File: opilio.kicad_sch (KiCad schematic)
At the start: 85 parts, among them J1 DB301V-5.0-2P, J2 USB_C_Receptacle_USB2.0, J6 Conn_01x06_Male, Q1 CJ3134KW, Q2 NCE30P30K, SW1 Reset, SW2 Boot, U1 EUP3458, U2 STM32F103C8T6, U3 USBLC6-2SC6, Y1 TAXM8M4RFDCET2T, Y2 YST310S 32.768KHz

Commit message: initial routing
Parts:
- removed J1: DB301V-5.0-2P, easyeda2kicad:CONN-TH_2P-P5.00_L7.6-W10.0, symbol easyeda:DB301V-5.0-2P
- added J1: SATA_Power_Connector, Custom:Sata_Power_Connector_SMD, symbol Custom:SATA_Power_Connector
- added J3: Conn_01x04_Male, Connector_PinHeader_2.54mm:PinHeader_1x04_P2.54mm_Vertical, symbol Connector:Conn_01x04_Male
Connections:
- net +12V: now also J1.13 (precharge_12V), J1.14 (12V), J1.15 (12V)
- net +3.3V: now also J3.1 (Pin_1)
- net GND: now also J1.10 (GND), J1.12 (GND), J1.4 (GND), J1.5 (GND), J1.6 (GND), J3.2 (Pin_2)
- net SWCLK: now also J3.3 (Pin_3)
- net SWIO: now also J3.4 (Pin_4)

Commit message: nearly ready
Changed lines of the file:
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@@
   (symbol (lib_id "Device:C_Small") (at 94.107 22.606 270) (unit 1)
     (in_bom yes) (on_board yes)
-    (property "Reference" "C5" (id 0) (at 94.996 17.907 0))
-    (property "Value" "10nF" (id 1) (at 92.964 18.161 0))
+    (property "Reference" "C5" (id 0) (at 93.726 17.145 90))
+    (property "Value" "10nF" (id 1) (at 93.98 19.177 90))
     (property "Footprint" "Capacitor_SMD:C_0402_1005Metric" (id 2) (at 94.107 22.606 0)
       (effects (font (size 1.27 1.27)) hide)

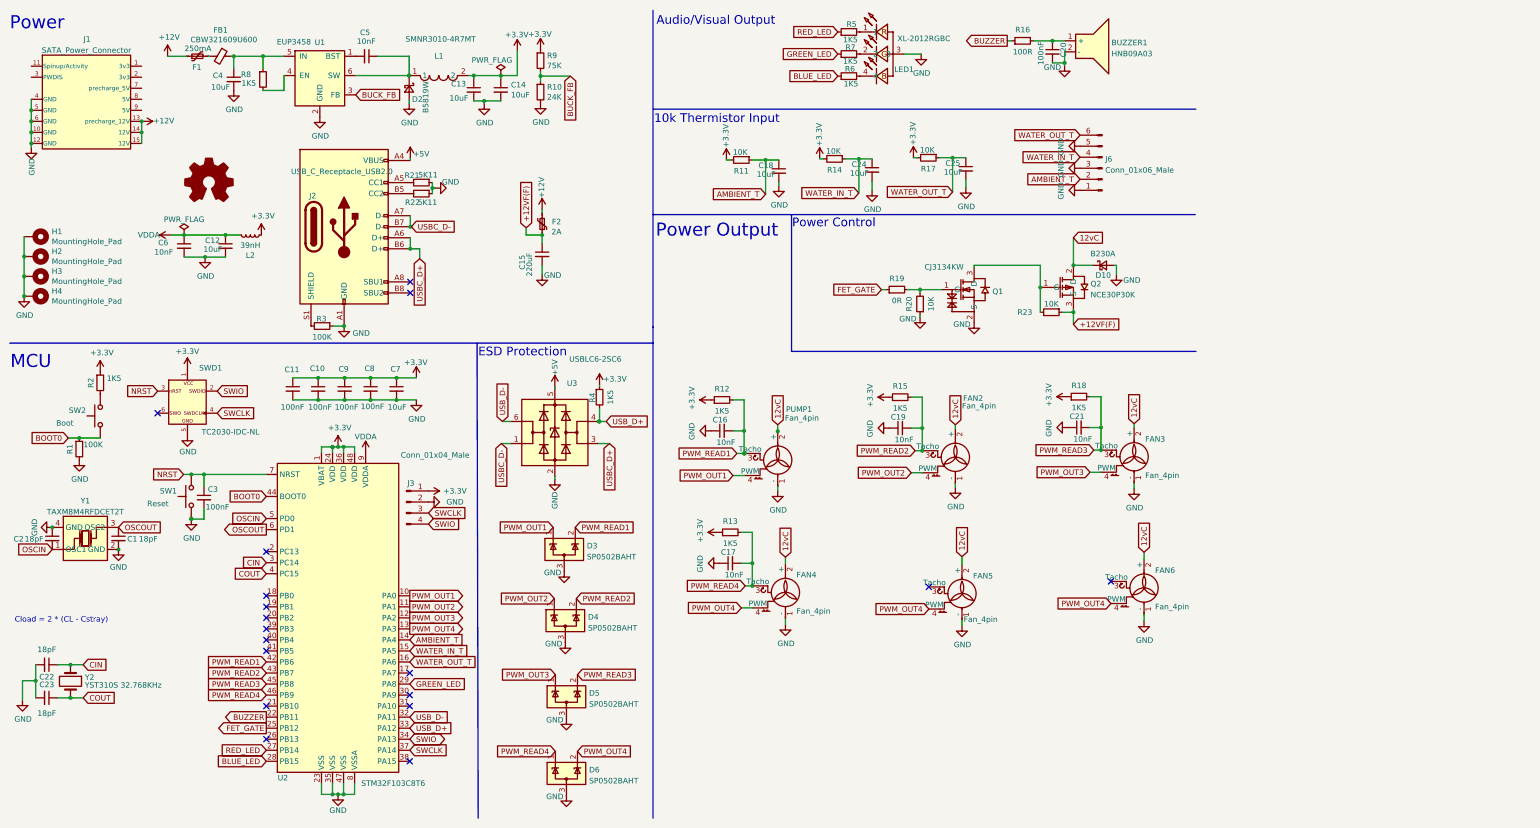
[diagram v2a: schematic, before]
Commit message: double mosfets
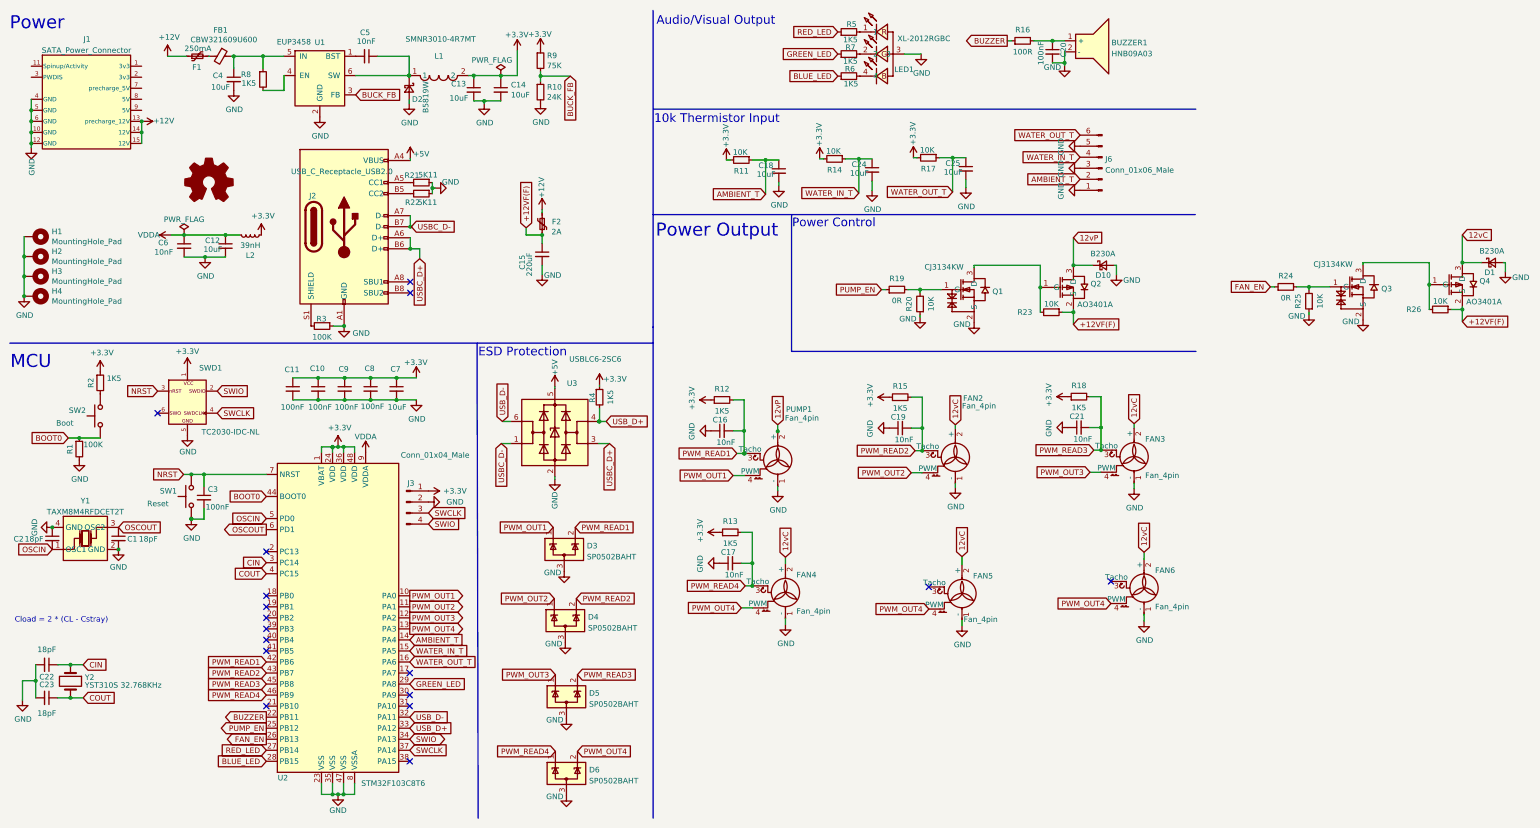
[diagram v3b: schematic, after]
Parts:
- removed Q2: NCE30P30K, easyeda2kicad:TO-252-2_L6.6-W6.1-P4.57-LS9.9-TL-CW, symbol easyeda:NCE30P30K
- added D1: B230A, Diode_SMD:D_SMA, symbol Device:D_Schottky_Small
- added Q2, Q4: AO3401A, easyeda2kicad:SOT-23_L2.9-W1.3-P1.90-LS2.4-BR, symbol easyeda:AO3401A
- added Q3: CJ3134KW, easyeda2kicad:SC-70-3_L2.1-W1.3-P1.30-LS2.1-BR, symbol easyeda:CJ3134KW
- added R24: 0R, Resistor_SMD:R_0402_1005Metric, symbol Device:R_Small
- added R25, R26: 10K, Resistor_SMD:R_0402_1005Metric, symbol Device:R_Small
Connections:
- net +12VF(F): now also Q2.2 (S), Q4.2 (S), R26.1
- net 12vC: now also D1.1 (K), Q4.3 (D); no longer D10.1 (K), PUMP1.2 (+)
- net GND: now also D1.2 (A), Q3.2 (S), R25.1
- net at Q1.3 (D), R23.2: now also Q2.1 (G)
- net FAN_EN: now reaches U2.26 (PB13)
- net FAN_EN: now also R24.1
- net FET_GATE renamed PUMP_EN
- new net: Q3.1 (G), R24.2, R25.2
- new net: Q3.3 (D), Q4.1 (G), R26.2
- new net 12vP: D10.1 (K), PUMP1.2 (+), Q2.3 (D)
- no-connect marks 18 -> 17

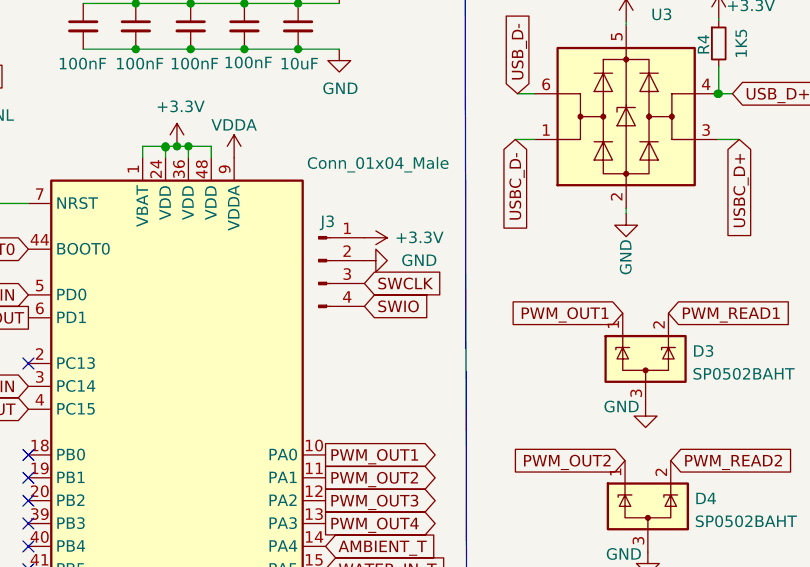
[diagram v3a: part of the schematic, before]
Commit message: match swd wires with bluepill
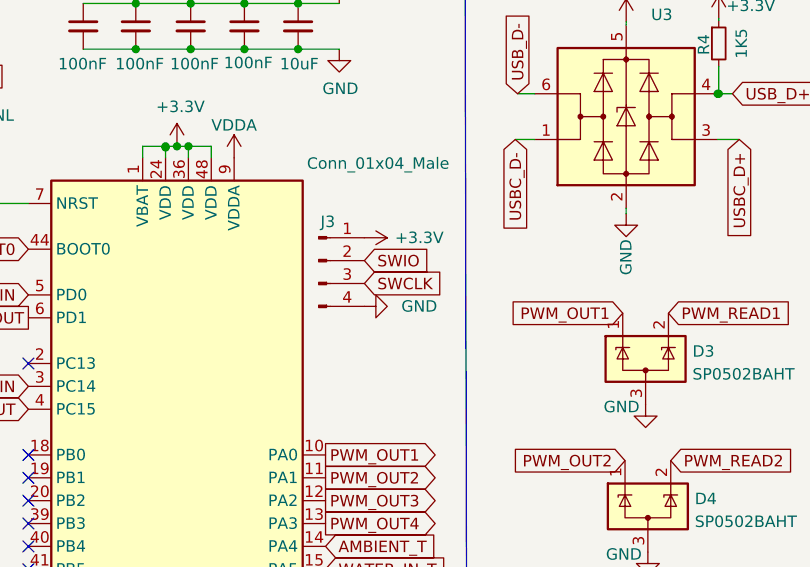
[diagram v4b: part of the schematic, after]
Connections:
- net GND: now also J3.4 (Pin_4); no longer J3.2 (Pin_2)
- net SWIO: now also J3.2 (Pin_2); no longer J3.4 (Pin_4)
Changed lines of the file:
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@@
     )
   )
-  (global_label "SWIO" (shape input) (at 108.331 130.302 0) (fields_autoplaced)
+  (global_label "SWIO" (shape input) (at 108.331 125.222 0) (fields_autoplaced)
     (effects (font (size 1.27 1.27)) (justify left))
-    (property "Intersheet References" "${INTERSHEET_REFS}" (id 0) (at 258.445 -146.812 0)
+    (property "Intersheet References" "${INTERSHEET_REFS}" (id 0) (at 258.445 -151.892 0)
       (effects (font (size 1.27 1.27)) hide)
     )
@@
     (pin "3")
   )
-  (symbol (lib_id "power:GND") (at 108.331 125.222 90) (unit 1)
+  (symbol (lib_id "power:GND") (at 108.331 130.302 90) (unit 1)
     (in_bom yes) (on_board yes)
-    (property "Reference" "#PWR06" (id 0) (at 114.681 125.222 0)
+    (property "Reference" "#PWR06" (id 0) (at 114.681 130.302 0)
       (effects (font (size 1.27 1.27)) hide)
     )
-    (property "Value" "GND" (id 1) (at 114.427 125.222 90))
-    (property "Footprint" "" (id 2) (at 108.331 125.222 0)
+    (property "Value" "GND" (id 1) (at 114.427 130.302 90))
+    (property "Footprint" "" (id 2) (at 108.331 130.302 0)
       (effects (font (size 1.27 1.27)) hide)
     )
-    (property "Datasheet" "" (id 3) (at 108.331 125.222 0)
+    (property "Datasheet" "" (id 3) (at 108.331 130.302 0)
       (effects (font (size 1.27 1.27)) hide)
     )

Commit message: before split schema
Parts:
- removed R2: 1K5, Resistor_SMD:R_0402_1005Metric, symbol Device:R_Small
- added C26: 100nF, Capacitor_SMD:C_0402_1005Metric, symbol Device:C_Small
- R1: value 100K -> 10K; LCSC Part C144792 -> C191123
- R3: value 100K -> 75K; LCSC Part C144792 -> C2689478
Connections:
- net +3.3V: now also SW2.2
- net BOOT0: now also C26.1
- net GND: now also C26.2
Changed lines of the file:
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@@
   (title_block
     (title "Opilio")
-    (date "2022-10-02")
-    (rev "6")
+    (date "2022-11-07")
+    (rev "7")
   )
   (junction (at 42.291 40.132) (diameter 0) (color 0 0 0 0)
@@
   (junction (at 221.488 76.327) (diameter 0) (color 0 0 0 0)
   )
+  (junction (at 32.766 110.49) (diameter 0) (color 0 0 0 0)
+  )
   (junction (at 104.14 66.929) (diameter 0) (color 0 0 0 0)
   )
@@
   (junction (at 180.975 108.839) (diameter 0) (color 0 0 0 0)
   )
+  (junction (at 30.226 115.57) (diameter 0) (color 0 0 0 0)
+  )
   (junction (at 16.891 42.672) (diameter 0) (color 0 0 0 0)
   )
@@
     (stroke (width 0) (type default) (color 0 0 0 0))
   )
+  (wire (pts (xy 30.226 115.57) (xy 27.94 115.57))
+    (stroke (width 0) (type default) (color 0 0 0 0))
+  )
   (wire (pts (xy 118.745 27.051) (xy 118.745 27.813))
     (stroke (width 0) (type default) (color 0 0 0 0))
@@
     (stroke (width 0) (type default) (color 0 0 0 0))
   )
+  (wire (pts (xy 30.226 115.57) (xy 32.766 115.57))
+    (stroke (width 0) (type default) (color 0 0 0 0))
+  )
   (wire (pts (xy 82.931 101.727) (xy 89.027 101.727))
     (stroke (width 0) (type default) (color 0 0 0 0))
@@
     (pin "1")
   )
-  (symbol (lib_id "power:GND") (at 27.94 115.57 0) (unit 1)
+  (symbol (lib_id "power:GND") (at 30.226 115.57 0) (unit 1)
     (in_bom yes) (on_board yes)
-    (property "Reference" "#PWR03" (id 0) (at 27.94 121.92 0)
+    (property "Reference" "#PWR03" (id 0) (at 30.226 121.92 0)
       (effects (font (size 1.27 1.27)) hide)
     )
-    (property "Value" "GND" (id 1) (at 28.067 119.9642 0))
-    (property "Footprint" "" (id 2) (at 27.94 115.57 0)
+    (property "Value" "GND" (id 1) (at 30.353 119.9642 0))
+    (property "Footprint" "" (id 2) (at 30.226 115.57 0)
       (effects (font (size 1.27 1.27)) hide)
     )
-    (property "Datasheet" "" (id 3) (at 27.94 115.57 0)
+    (property "Datasheet" "" (id 3) (at 30.226 115.57 0)
       (effects (font (size 1.27 1.27)) hide)
     )
@@
     (pin "1")
   )
-  (symbol (lib_id "power:+3.3V") (at 32.766 95.25 0) (unit 1)
+  (symbol (lib_id "power:+3.3V") (at 32.766 100.33 0) (unit 1)
     (in_bom yes) (on_board yes)
-    (property "Reference" "#PWR05" (id 0) (at 32.766 99.06 0)
+    (property "Reference" "#PWR05" (id 0) (at 32.766 104.14 0)
       (effects (font (size 1.27 1.27)) hide)
     )
-    (property "Value" "+3.3V" (id 1) (at 33.147 90.8558 0))
-    (property "Footprint" "" (id 2) (at 32.766 95.25 0)
+    (property "Value" "+3.3V" (id 1) (at 33.147 95.9358 0))
+    (property "Footprint" "" (id 2) (at 32.766 100.33 0)
       (effects (font (size 1.27 1.27)) hide)
     )
-    (property "Datasheet" "" (id 3) (at 32.766 95.25 0)
+    (property "Datasheet" "" (id 3) (at 32.766 100.33 0)
       (effects (font (size 1.27 1.27)) hide)
     )
@@
     (in_bom yes) (on_board yes)
     (property "Reference" "R3" (id 0) (at 83.693 83.058 90))
-    (property "Value" "100K" (id 1) (at 83.82 87.249 90))
+    (property "Value" "75K" (id 1) (at 83.82 87.249 90))
     (property "Footprint" "Resistor_SMD:R_0402_1005Metric" (id 2) (at 83.82 84.709 0)
       (effects (font (size 1.27 1.27)) hide)
@@
       (effects (font (size 1.27 1.27)) hide)
     )
-    (property "LCSC Part" "C144792" (id 4) (at 83.82 84.709 0)
+    (property "LCSC Part" "C2689478" (id 4) (at 83.82 84.709 0)
       (effects (font (size 1.27 1.27)) hide)
     )
@@
     (pin "2")
   )
+  (symbol (lib_id "Device:C_Small") (at 32.766 113.03 0) (unit 1)
+    (in_bom yes) (on_board yes)
+    (property "Reference" "C26" (id 0) (at 33.655 111.125 0)
+      (effects (font (size 1.27 1.27)) (justify left))
+    )
+    (property "Value" "100nF" (id 1) (at 33.147 115.189 0)
+      (effects (font (size 1.27 1.27)) (justify left))
+    )
+    (property "Footprint" "Capacitor_SMD:C_0402_1005Metric" (id 2) (at 32.766 113.03 0)
+      (effects (font (size 1.27 1.27)) hide)
+    )
+    (property "Datasheet" "~" (id 3) (at 32.766 113.03 0)
+      (effects (font (size 1.27 1.27)) hide)
+    )
+    (property "LCSC Part" "C100072" (id 4) (at 32.766 113.03 0)
+      (effects (font (size 1.27 1.27)) hide)
+    )
+    (pin "1")
+    (pin "2")
+  )
   (symbol (lib_id "Device:C_Small") (at 177.8 139.319 90) (unit 1)
     (in_bom yes) (on_board yes)
@@
     (in_bom yes) (on_board yes)
     (property "Reference" "R1" (id 0) (at 25.781 113.03 90))
-    (property "Value" "100K" (id 1) (at 31.115 112.014 0))
+    (property "Value" "10K" (id 1) (at 24.257 115.189 0))
     (property "Footprint" "Resistor_SMD:R_0402_1005Metric" (id 2) (at 27.94 113.03 0)
       (effects (font (size 1.27 1.27)) hide)
@@
       (effects (font (size 1.27 1.27)) hide)
     )
-    (property "LCSC Part" "C144792" (id 4) (at 27.94 113.03 0)
+    (property "LCSC Part" "C191123" (id 4) (at 27.94 113.03 0)
       (effects (font (size 1.27 1.27)) hide)
     )
@@
     (pin "2")
   )
-  (symbol (lib_id "Device:R_Small") (at 32.766 97.79 0) (unit 1)
-    (in_bom yes) (on_board yes)
-    (property "Reference" "R2" (id 0) (at 30.607 97.79 90))
-    (property "Value" "1K5" (id 1) (at 35.941 96.774 0))
-    (property "Footprint" "Resistor_SMD:R_0402_1005Metric" (id 2) (at 32.766 97.79 0)
-      (effects (font (size 1.27 1.27)) hide)
-    )
-    (property "Datasheet" "~" (id 3) (at 32.766 97.79 0)
-      (effects (font (size 1.27 1.27)) hide)
-    )
-    (property "LCSC Part" "C413084" (id 4) (at 32.766 97.79 0)
-      (effects (font (size 1.27 1.27)) hide)
-    )
-    (pin "1")
-    (pin "2")
-  )
   (symbol (lib_id "power:GND") (at 173.355 108.839 270) (unit 1)
     (in_bom yes) (on_board yes)
@@
       (reference "C25") (unit 1) (value "10uF") (footprint "Capacitor_SMD:C_0603_1608Metric")
     )
+    (path "/7a3f805d-442c-4192-9b77-8a7b61bfd9f5"
+      (reference "C26") (unit 1) (value "100nF") (footprint "Capacitor_SMD:C_0402_1005Metric")
+    )
     (path "/ff43c545-2e78-4ffc-ac31-897951bdbe96"
       (reference "D1") (unit 1) (value "B230A") (footprint "Diode_SMD:D_SMA")
@@
     )
     (path "/be987873-4856-4ad7-aaee-745ffdc5e733"
-      (reference "R1") (unit 1) (value "100K") (footprint "Resistor_SMD:R_0402_1005Metric")
-    )
-    (path "/c8fa8fa3-be95-4a0c-bb19-a1e338cef170"
-      (reference "R2") (unit 1) (value "1K5") (footprint "Resistor_SMD:R_0402_1005Metric")
+      (reference "R1") (unit 1) (value "10K") (footprint "Resistor_SMD:R_0402_1005Metric")
     )
     (path "/61dbdb34-0154-4f93-a2b2-aaae1dfa3913"
-      (reference "R3") (unit 1) (value "100K") (footprint "Resistor_SMD:R_0402_1005Metric")
+      (reference "R3") (unit 1) (value "75K") (footprint "Resistor_SMD:R_0402_1005Metric")
     )
     (path "/beb113ce-d7fe-47cb-97e6-be05f9ef150e"
